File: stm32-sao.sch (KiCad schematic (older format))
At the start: 41 parts, among them J1 Conn_02x02_Top_Bottom, J2 Conn_02x04_Top_Bottom, J3 Conn_01x04, J4 Conn_01x12_Male, U1 STM32F030F4Px, U2 M24C02-WMN

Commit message: fix: use male connector for SAO
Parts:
- J1: footprint Connector_PinSocket_2.54mm:PinSocket_2x02_P2.54mm_Vertical -> Connector_PinHeader_2.54mm:PinHeader_2x02_P2.54mm_Vertical
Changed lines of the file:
@@
 F 0 "J1" H 4850 5817 50  0000 C CNN
 F 1 "Conn_02x02_Top_Bottom" H 4850 5726 50  0000 C CNN
-F 2 "Connector_PinSocket_2.54mm:PinSocket_2x02_P2.54mm_Vertical" H 4800 5600 50  0001 C CNN
+F 2 "Connector_PinHeader_2.54mm:PinHeader_2x02_P2.54mm_Vertical" H 4800 5600 50  0001 C CNN
 F 3 "~" H 4800 5600 50  0001 C CNN
 F 4 "0" H 4800 5600 50  0001 C CNN "JLCPCB BOM"

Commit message: fix: LEDs connected wrong
they should be connected to VCC, not GND!
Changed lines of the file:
@@
 	1    0    0    -1
-$EndComp
-$Comp
-L power:GND #PWR0118
-U 1 1 5D9D573D
-P 8850 3750
-F 0 "#PWR0118" H 8850 3500 50  0001 C CNN
-F 1 "GND" V 8855 3622 50  0000 R CNN
-F 2 "" H 8850 3750 50  0001 C CNN
-F 3 "" H 8850 3750 50  0001 C CNN
-	1    8850 3750
-	0    -1   -1   0
 $EndComp
 Wire Wire Line
@@
 	1    0    0    -1
 $EndComp
+$Comp
+L power:VDD #PWR?
+U 1 1 5DA37260
+P 8850 3750
+F 0 "#PWR?" H 8850 3600 50  0001 C CNN
+F 1 "VDD" V 8868 3877 50  0000 L CNN
+F 2 "" H 8850 3750 50  0001 C CNN
+F 3 "" H 8850 3750 50  0001 C CNN
+	1    8850 3750
+	0    1    1    0
+$EndComp
 $EndSCHEMATC

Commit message: fix: wrong I2C pins
PA9/PA10 should be connected to the I2C bus instead of PF0/PF1
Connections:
- net labels added: LED10, LED9
- wire segments 118 -> 122
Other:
- moved on the sheet: JP9, R12, R13
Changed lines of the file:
@@
 Wire Wire Line
 	4850 4600 4850 4950
-Text Label 4000 4100 0    50   ~ 0
+Text Label 4100 4900 0    50   ~ 0
 SDA
-Text Label 4000 4200 0    50   ~ 0
+Text Label 4100 5000 0    50   ~ 0
 SCL
 $Comp
@@
 	6050 4000 5350 4000
 Wire Wire Line
-	5350 4100 6050 4100
-Wire Wire Line
 	6600 5600 6250 5600
 Text Label 6300 5600 0    50   ~ 0
@@
 $EndComp
 Wire Wire Line
-	5350 4200 6050 4200
-Connection ~ 6050 4200
-Wire Wire Line
 	6050 4200 6650 4200
-Wire Wire Line
-	6650 4100 6050 4100
-Connection ~ 6050 4100
 Wire Wire Line
 	6650 4000 6050 4000
@@
 L Device:R R12
 U 1 1 5DA13144
-P 3700 4100
-F 0 "R12" V 3800 4100 50  0000 C CNN
-F 1 "10k" V 3700 4100 50  0000 C CNN
-F 2 "Resistor_SMD:R_0603_1608Metric" V 3630 4100 50  0001 C CNN
-F 3 "~" H 3700 4100 50  0001 C CNN
-	1    3700 4100
-	0    -1   -1   0
-$EndComp
-Wire Wire Line
-	3850 4100 4350 4100
+P 3800 4900
+F 0 "R12" V 3900 4900 50  0000 C CNN
+F 1 "10k" V 3800 4900 50  0000 C CNN
+F 2 "Resistor_SMD:R_0603_1608Metric" V 3730 4900 50  0001 C CNN
+F 3 "~" H 3800 4900 50  0001 C CNN
+	1    3800 4900
+	0    -1   -1   0
+$EndComp
 $Comp
 L Device:R R13
 U 1 1 5DA1D6FC
-P 3700 4200
-F 0 "R13" V 3600 4200 50  0000 C CNN
-F 1 "10k" V 3700 4200 50  0000 C CNN
-F 2 "Resistor_SMD:R_0603_1608Metric" V 3630 4200 50  0001 C CNN
-F 3 "~" H 3700 4200 50  0001 C CNN
-	1    3700 4200
-	0    -1   -1   0
-$EndComp
-Wire Wire Line
-	3850 4200 4350 4200
+P 3800 5000
+F 0 "R13" V 3700 5000 50  0000 C CNN
+F 1 "10k" V 3800 5000 50  0000 C CNN
+F 2 "Resistor_SMD:R_0603_1608Metric" V 3730 5000 50  0001 C CNN
+F 3 "~" H 3800 5000 50  0001 C CNN
+	1    3800 5000
+	0    -1   -1   0
+$EndComp
 $Comp
 L power:VDD #PWR0119
 U 1 1 5DA221FC
-P 3000 4150
-F 0 "#PWR0119" H 3000 4000 50  0001 C CNN
-F 1 "VDD" V 3018 4277 50  0000 L CNN
-F 2 "" H 3000 4150 50  0001 C CNN
-F 3 "" H 3000 4150 50  0001 C CNN
-	1    3000 4150
+P 3000 4750
+F 0 "#PWR0119" H 3000 4600 50  0001 C CNN
+F 1 "VDD" V 3018 4877 50  0000 L CNN
+F 2 "" H 3000 4750 50  0001 C CNN
+F 3 "" H 3000 4750 50  0001 C CNN
+	1    3000 4750
 	0    -1   -1   0
 $EndComp
@@
 L Jumper:SolderJumper_2_Bridged JP9
 U 1 1 5DA24097
-P 3300 4150
-F 0 "JP9" H 3300 4355 50  0000 C CNN
-F 1 "I2C_PULLUP" H 3300 4264 50  0000 C CNN
-F 2 "Jumper:SolderJumper-2_P1.3mm_Bridged_Pad1.0x1.5mm" H 3300 4150 50  0001 C CNN
-F 3 "~" H 3300 4150 50  0001 C CNN
-F 4 "0" H 3300 4150 50  0001 C CNN "JLCPCB BOM"
-	1    3300 4150
-	1    0    0    -1
-$EndComp
-Wire Wire Line
-	3550 4100 3550 4150
-Wire Wire Line
-	3450 4150 3550 4150
-Connection ~ 3550 4150
-Wire Wire Line
-	3550 4150 3550 4200
-Wire Wire Line
-	3150 4150 3050 4150
+P 3400 4950
+F 0 "JP9" H 3400 5155 50  0000 C CNN
+F 1 "I2C_PULLUP" H 3400 5064 50  0000 C CNN
+F 2 "Jumper:SolderJumper-2_P1.3mm_Bridged_Pad1.0x1.5mm" H 3400 4950 50  0001 C CNN
+F 3 "~" H 3400 4950 50  0001 C CNN
+F 4 "0" H 3400 4950 50  0001 C CNN "JLCPCB BOM"
+	1    3400 4950
+	1    0    0    -1
+$EndComp
+Wire Wire Line
+	3650 4900 3650 4950
+Wire Wire Line
+	3550 4950 3650 4950
+Connection ~ 3650 4950
+Wire Wire Line
+	3650 4950 3650 5000
 $Comp
 L Device:R R14
@@
 Wire Wire Line
 	3850 4400 3850 4600
-Wire Wire Line
-	3050 4150 3050 4600
-Wire Wire Line
-	3050 4600 3550 4600
-Connection ~ 3050 4150
-Wire Wire Line
-	3050 4150 3000 4150
 $Comp
 L Connector_Generic:Conn_02x02_Top_Bottom J1
@@
 	0    1    1    0
 $EndComp
+Text Label 5400 4200 0    50   ~ 0
+SDA
+Text Label 5400 4100 0    50   ~ 0
+SCL
+Wire Wire Line
+	5350 4100 5550 4100
+Wire Wire Line
+	5350 4200 5550 4200
+Wire Wire Line
+	6050 4200 5750 4200
+Connection ~ 6050 4200
+Connection ~ 6050 4100
+Wire Wire Line
+	6650 4100 6050 4100
+Wire Wire Line
+	5750 4100 6050 4100
+Text Label 5800 4100 0    50   ~ 0
+LED9
+Text Label 5800 4200 0    50   ~ 0
+LED10
+Wire Wire Line
+	3250 4950 3000 4950
+Wire Wire Line
+	3000 4950 3000 4750
+Wire Wire Line
+	3000 4600 3000 4750
+Wire Wire Line
+	3000 4600 3550 4600
+Connection ~ 3000 4750
+Wire Wire Line
+	3950 4900 4250 4900
+Wire Wire Line
+	3950 5000 4250 5000
+Wire Wire Line
+	4350 4100 4100 4100
+Wire Wire Line
+	4350 4200 4100 4200
+Text Label 4100 4100 0    50   ~ 0
+LED9
+Text Label 4100 4200 0    50   ~ 0
+LED10
 $EndSCHEMATC

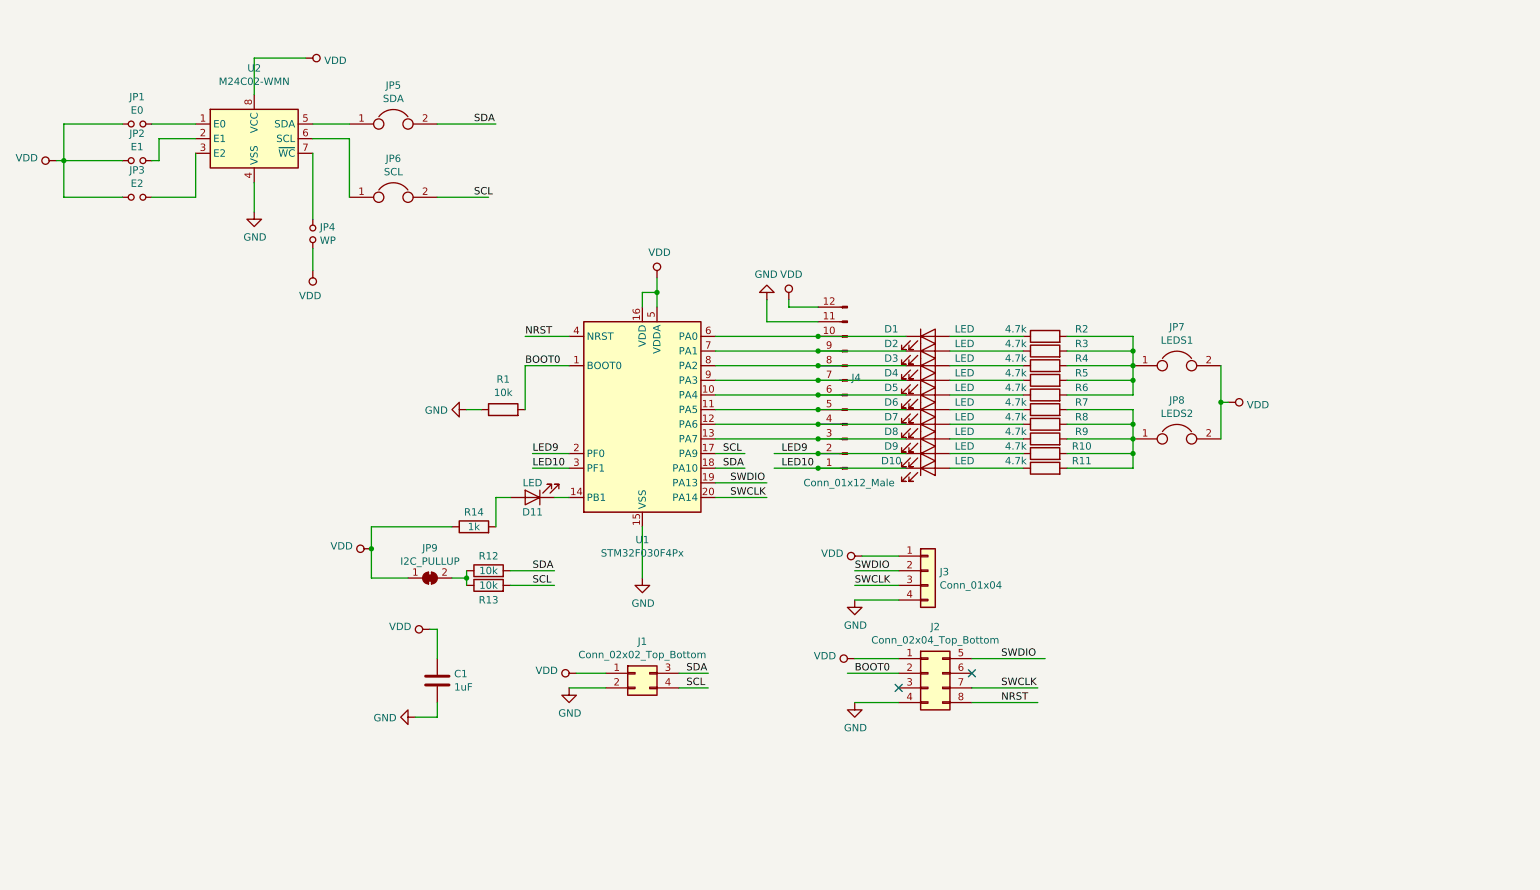
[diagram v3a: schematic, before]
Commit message: feat: second version of the PCB
1. Upgrade #badgelife Shitty Add-On connector to V1.69bis
2. Add 10 NeoPixels (WS2812B-Mini)
3. Add a small 7mm speaker
4. Redesign the board
5. Add a second I2C EEPROM
6. Add AramCon conference logo
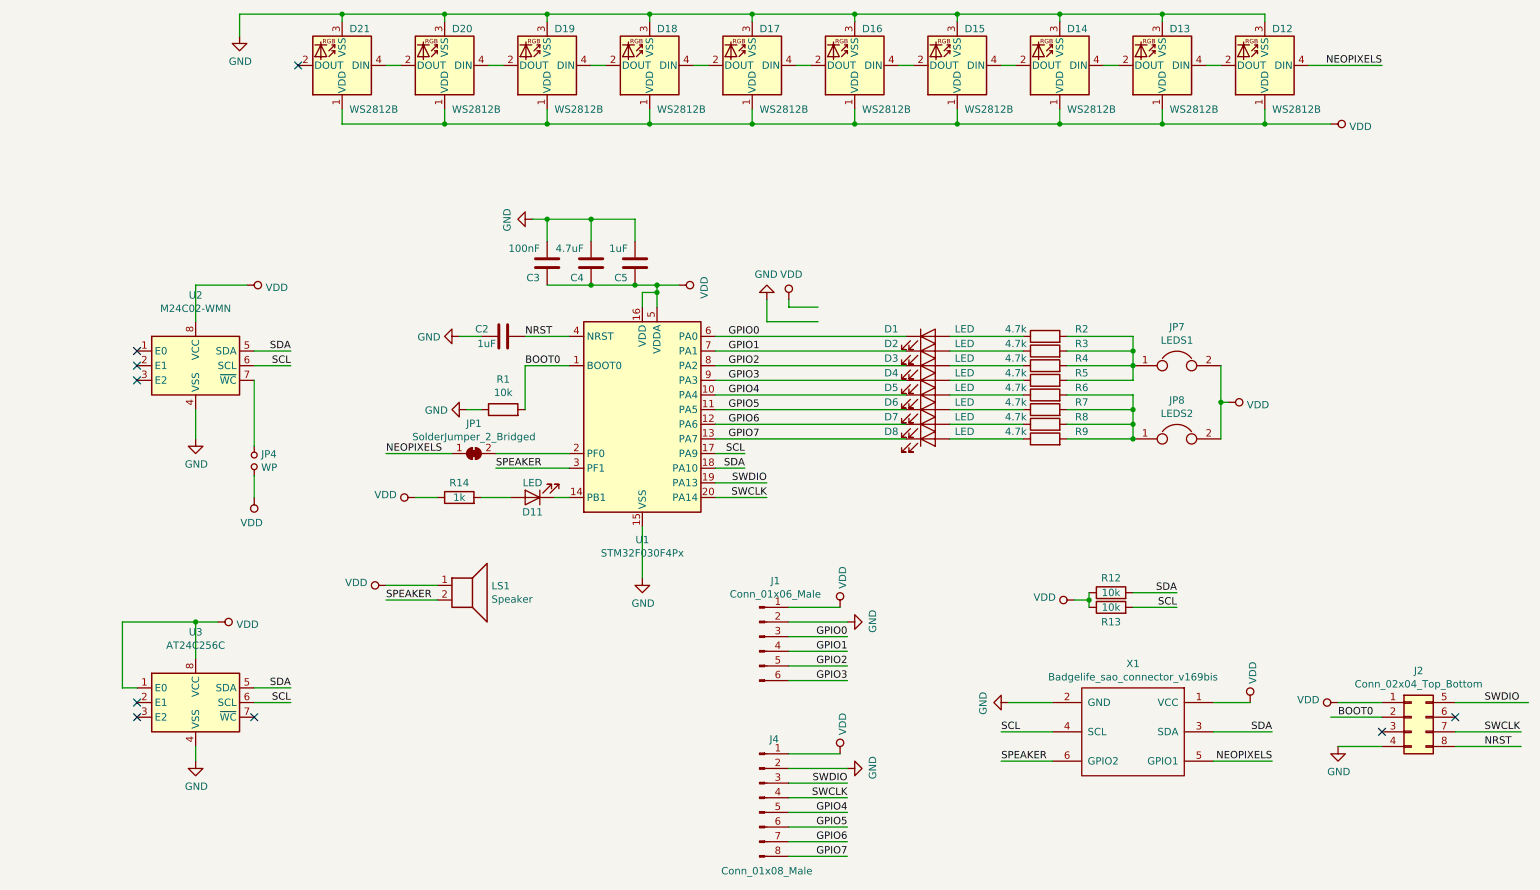
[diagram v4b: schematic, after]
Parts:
- removed C1: 1uF, Capacitor_SMD:C_0603_1608Metric, symbol Device:C
- removed D10, D9: LED, LED_SMD:LED_0603_1608Metric, symbol Device:LED
- removed J1: Conn_02x02_Top_Bottom, Connector_PinHeader_2.54mm:PinHeader_2x02_P2.54mm_Vertical, symbol Connector_Generic:Conn_02x02_Top_Bottom
- removed J3: Conn_01x04, Connector_PinHeader_2.54mm:PinHeader_1x04_P2.54mm_Vertical, symbol Connector_Generic:Conn_01x04
- removed J4: Conn_01x12_Male, Connector_PinHeader_2.54mm:PinHeader_1x12_P2.54mm_Vertical, symbol Connector:Conn_01x12_Male
- removed JP1: E0, Jumper:SolderJumper-2_P1.3mm_Open_RoundedPad1.0x1.5mm, symbol Device:Jumper_NO_Small
- removed JP2: E1, Jumper:SolderJumper-2_P1.3mm_Open_RoundedPad1.0x1.5mm, symbol Device:Jumper_NO_Small
- removed JP3: E2, Jumper:SolderJumper-2_P1.3mm_Open_RoundedPad1.0x1.5mm, symbol Device:Jumper_NO_Small
- removed JP5: SDA, Jumper:SolderJumper-2_P1.3mm_Bridged_Pad1.0x1.5mm, symbol Device:Jumper
- removed JP6: SCL, Jumper:SolderJumper-2_P1.3mm_Bridged_Pad1.0x1.5mm, symbol Device:Jumper
- removed JP9: I2C_PULLUP, Jumper:SolderJumper-2_P1.3mm_Bridged_Pad1.0x1.5mm, symbol Jumper:SolderJumper_2_Bridged
- removed R10, R11: 4.7k, Resistor_SMD:R_0603_1608Metric, symbol Device:R
- added C2, C5: 1uF, Capacitor_SMD:C_0402_1005Metric, symbol Device:C
- added C3: 100nF, Capacitor_SMD:C_0402_1005Metric, symbol Device:C
- added C4: 4.7uF, Capacitor_SMD:C_0402_1005Metric, symbol Device:C
- added D12, D13, D14, D15, D16, D17, D18, D19, D20, D21: WS2812B, AramCon:LED-SMD_4P-L3.5-W3.5-TL_WS2812B, symbol LED:WS2812B
- added J1: Conn_01x06_Male, Connector_PinHeader_2.54mm:PinHeader_1x06_P2.54mm_Vertical, symbol Connector:Conn_01x06_Male
- added J4: Conn_01x08_Male, Connector_PinHeader_2.54mm:PinHeader_1x08_P2.54mm_Vertical, symbol Connector:Conn_01x08_Male
- added JP1: SolderJumper_2_Bridged, Jumper:SolderJumper-2_P1.3mm_Bridged_Pad1.0x1.5mm, symbol Jumper:SolderJumper_2_Bridged
- added LS1: Speaker, AramCon:BUZZER-R14-2P-7.6PITCH, symbol Device:Speaker
- added U3: AT24C256C, Package_SO:SOIC-8_3.9x4.9mm_P1.27mm, symbol Memory_EEPROM:M24C02-WMN
- added X1: Badgelife_sao_connector_v169bis, AramCon:Badgelife-SAOv169-SAO-2x3, symbol badgelife_shitty_addon_v169bis:Badgelife_sao_connector_v169bis
- R1: footprint Resistor_SMD:R_0603_1608Metric -> Resistor_SMD:R_0402_1005Metric; LCSC Part C25804 -> C25744
- R12, R13, R3, R4, R5, R6, R7, R8, R9: footprint Resistor_SMD:R_0603_1608Metric -> Resistor_SMD:R_0402_1005Metric
- R2: footprint Resistor_SMD:R_0603_1608Metric -> Resistor_SMD:R_0402_1005Metric; LCSC Part C23162 -> C25900
- U1: LCSC Part C32908 -> C89040
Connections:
- net labels added: GPIO0, GPIO1, GPIO2, GPIO3, GPIO4, GPIO5, GPIO6, GPIO7, NEOPIXELS, SPEAKER
- net labels removed: LED10, LED9
- wire segments 122 -> 166
- no-connect marks 2 -> 9
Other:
- moved on the sheet: J2, JP4, R12, R13, R14, U2
